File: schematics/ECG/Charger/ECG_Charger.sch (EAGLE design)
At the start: 7 parts, among them IC1 MCP73832_SOT23-5

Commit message: routed charger board
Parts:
- added C2: 4.7uF, rcl:C-USC0805
- added CONN1: M80-4V, harwin:M80-4V
- added CONN2: M80-6V, harwin:M80-6V
- C1: device rcl:C-USC0402 -> rcl:C-USC0805
- R1, R2: device rcl:R-US_R0201 -> rcl:R-US_R0805
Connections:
- removed net VSS: R2.1
- net BATT: now also C2.1, CONN1.3
- net GND: now also C2.2, CONN1.4, R2.1
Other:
- moved on the sheet: C1, FUSE, IC1, LED1, R1, R2, USBCONN

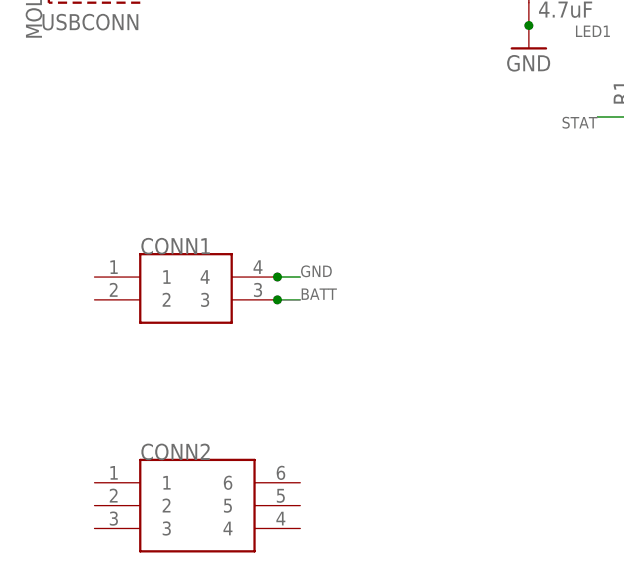
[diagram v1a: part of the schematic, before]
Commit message: switched ECG boards to spring loaded pin headers
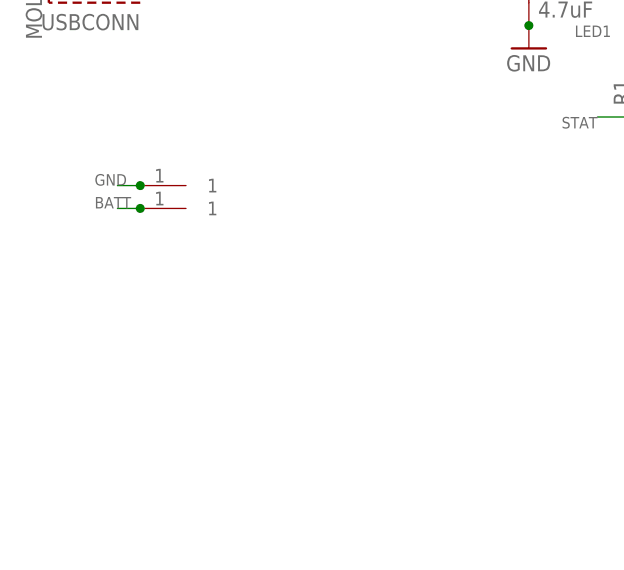
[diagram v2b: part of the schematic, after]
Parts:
- removed CONN1: M80-4V, harwin:M80-4V
- removed CONN2: M80-6V, harwin:M80-6V
- added U$1, U$2: PISTON_RA_TH, pins:PISTON_RA_TH
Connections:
- net BATT: now also U$1.1; no longer CONN1.3
- net GND: now also U$2.1; no longer CONN1.4
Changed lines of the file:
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@@
 <?xml version="1.0" encoding="utf-8"?>
 <!DOCTYPE eagle SYSTEM "eagle.dtd">
-<eagle version="6.4">
+<eagle version="6.5.0">
 <drawing>
 <settings>
@@
 <grid distance="0.1" unitdist="inch" unit="inch" style="lines" multiple="1" display="no" altdistance="0.01" altunitdist="inch" altunit="inch"/>
 <layers>
-<layer number="1" name="Top" color="4" fill="1" visible="yes" active="no"/>
-<layer number="2" name="Route2" color="1" fill="3" visible="yes" active="no"/>
-<layer number="3" name="Route3" color="4" fill="3" visible="yes" active="no"/>
-<layer number="4" name="Route4" color="1" fill="4" visible="yes" active="no"/>
-<layer number="5" name="Route5" color="4" fill="4" visible="yes" active="no"/>
-<layer number="6" name="Route6" color="1" fill="8" visible="yes" active="no"/>
-<layer number="7" name="Route7" color="4" fill="8" visible="yes" active="no"/>
-<layer number="8" name="Route8" color="1" fill="2" visible="yes" active="no"/>
-<layer number="9" name="Route9" color="4" fill="2" visible="yes" active="no"/>
-<layer number="10" name="Route10" color="1" fill="7" visible="yes" active="no"/>
-<layer number="11" name="Route11" color="4" fill="7" visible="yes" active="no"/>
-<layer number="12" name="Route12" color="1" fill="5" visible="yes" active="no"/>
-<layer number="13" name="Route13" color="4" fill="5" visible="yes" active="no"/>
-<layer number="14" name="Route14" color="1" fill="6" visible="yes" active="no"/>
-<layer number="15" name="Route15" color="4" fill="6" visible="yes" active="no"/>
-<layer number="16" name="Bottom" color="1" fill="1" visible="yes" active="no"/>
-<layer number="17" name="Pads" color="2" fill="1" visible="yes" active="no"/>
-<layer number="18" name="Vias" color="2" fill="1" visible="yes" active="no"/>
-<layer number="19" name="Unrouted" color="6" fill="1" visible="yes" active="no"/>
-<layer number="20" name="Dimension" color="15" fill="1" visible="yes" active="no"/>
-<layer number="21" name="tPlace" color="7" fill="1" visible="yes" active="no"/>
-<layer number="22" name="bPlace" color="7" fill="1" visible="yes" active="no"/>
-<layer number="23" name="tOrigins" color="15" fill="1" visible="yes" active="no"/>
-<layer number="24" name="bOrigins" color="15" fill="1" visible="yes" active="no"/>
-<layer number="25" name="tNames" color="7" fill="1" visible="yes" active="no"/>
-<layer number="26" name="bNames" color="7" fill="1" visible="yes" active="no"/>
-<layer number="27" name="tValues" color="7" fill="1" visible="yes" active="no"/>
-<layer number="28" name="bValues" color="7" fill="1" visible="yes" active="no"/>
+<layer number="1" name="Top" color="4" fill="1" visible="no" active="no"/>
+<layer number="2" name="Route2" color="1" fill="3" visible="no" active="no"/>
+<layer number="3" name="Route3" color="4" fill="3" visible="no" active="no"/>
+<layer number="4" name="Route4" color="1" fill="4" visible="no" active="no"/>
+<layer number="5" name="Route5" color="4" fill="4" visible="no" active="no"/>
+<layer number="6" name="Route6" color="1" fill="8" visible="no" active="no"/>
+<layer number="7" name="Route7" color="4" fill="8" visible="no" active="no"/>
+<layer number="8" name="Route8" color="1" fill="2" visible="no" active="no"/>
+<layer number="9" name="Route9" color="4" fill="2" visible="no" active="no"/>
+<layer number="10" name="Route10" color="1" fill="7" visible="no" active="no"/>
+<layer number="11" name="Route11" color="4" fill="7" visible="no" active="no"/>
+<layer number="12" name="Route12" color="1" fill="5" visible="no" active="no"/>
+<layer number="13" name="Route13" color="4" fill="5" visible="no" active="no"/>
+<layer number="14" name="Route14" color="1" fill="6" visible="no" active="no"/>
+<layer number="15" name="Route15" color="4" fill="6" visible="no" active="no"/>
+<layer number="16" name="Bottom" color="1" fill="1" visible="no" active="no"/>
+<layer number="17" name="Pads" color="2" fill="1" visible="no" active="no"/>
+<layer number="18" name="Vias" color="2" fill="1" visible="no" active="no"/>
+<layer number="19" name="Unrouted" color="6" fill="1" visible="no" active="no"/>
+<layer number="20" name="Dimension" color="15" fill="1" visible="no" active="no"/>
+<layer number="21" name="tPlace" color="7" fill="1" visible="no" active="no"/>
+<layer number="22" name="bPlace" color="7" fill="1" visible="no" active="no"/>
+<layer number="23" name="tOrigins" color="15" fill="1" visible="no" active="no"/>
+<layer number="24" name="bOrigins" color="15" fill="1" visible="no" active="no"/>
+<layer number="25" name="tNames" color="7" fill="1" visible="no" active="no"/>
+<layer number="26" name="bNames" color="7" fill="1" visible="no" active="no"/>
+<layer number="27" name="tValues" color="7" fill="1" visible="no" active="no"/>
+<layer number="28" name="bValues" color="7" fill="1" visible="no" active="no"/>
 <layer number="29" name="tStop" color="7" fill="3" visible="no" active="no"/>
 <layer number="30" name="bStop" color="7" fill="6" visible="no" active="no"/>
@@
 <layer number="35" name="tGlue" color="7" fill="4" visible="no" active="no"/>
 <layer number="36" name="bGlue" color="7" fill="5" visible="no" active="no"/>
-<layer number="37" name="tTest" color="7" fill="1" visible="yes" active="no"/>
-<layer number="38" name="bTest" color="7" fill="1" visible="yes" active="no"/>
+<layer number="37" name="tTest" color="7" fill="1" visible="no" active="no"/>
+<layer number="38" name="bTest" color="7" fill="1" visible="no" active="no"/>
 <layer number="39" name="tKeepout" color="4" fill="11" visible="no" active="no"/>
 <layer number="40" name="bKeepout" color="1" fill="11" visible="no" active="no"/>
@@
 <layer number="44" name="Drills" color="7" fill="1" visible="no" active="no"/>
 <layer number="45" name="Holes" color="7" fill="1" visible="no" active="no"/>
-<layer number="46" name="Milling" color="3" fill="1" visible="yes" active="no"/>
-<layer number="47" name="Measures" color="7" fill="1" visible="yes" active="no"/>
-<layer number="48" name="Document" color="7" fill="1" visible="yes" active="no"/>
-<layer number="49" name="Reference" color="7" fill="1" visible="yes" active="no"/>
-<layer number="50" name="dxf" color="7" fill="1" visible="yes" active="no"/>
-<layer number="51" name="tDocu" color="7" fill="1" visible="yes" active="no"/>
-<layer number="52" name="bDocu" color="7" fill="1" visible="yes" active="no"/>
-<layer number="53" name="tGND_GNDA" color="7" fill="9" visible="yes" active="no"/>
-<layer number="54" name="bGND_GNDA" color="1" fill="9" visible="yes" active="no"/>
-<layer number="56" name="wert" color="7" fill="1" visible="yes" active="no"/>
+<layer number="46" name="Milling" color="3" fill="1" visible="no" active="no"/>
+<layer number="47" name="Measures" color="7" fill="1" visible="no" active="no"/>
+<layer number="48" name="Document" color="7" fill="1" visible="no" active="no"/>
+<layer number="49" name="Reference" color="7" fill="1" visible="no" active="no"/>
+<layer number="50" name="dxf" color="7" fill="1" visible="no" active="no"/>
+<layer number="51" name="tDocu" color="7" fill="1" visible="no" active="no"/>
+<layer number="52" name="bDocu" color="7" fill="1" visible="no" active="no"/>
+<layer number="53" name="tGND_GNDA" color="7" fill="9" visible="no" active="no"/>
+<layer number="54" name="bGND_GNDA" color="1" fill="9" visible="no" active="no"/>
+<layer number="56" name="wert" color="7" fill="1" visible="no" active="no"/>
 <layer number="91" name="Nets" color="2" fill="1" visible="yes" active="yes"/>
 <layer number="92" name="Busses" color="1" fill="1" visible="yes" active="yes"/>
@@
 <part name="C2" library="rcl" deviceset="C-US" device="C0805" value="4.7uF"/>
 <part name="GND1" library="supply1" deviceset="GND" device=""/>
-<part name="CONN2" library="harwin" deviceset="M80-6" device="V"/>
-<part name="CONN1" library="harwin" deviceset="M80-4" device="V"/>
 <part name="GND3" library="supply1" deviceset="GND" device=""/>
+<part name="U$1" library="pins" deviceset="PISTON_RA_TH" device=""/>
+<part name="U$2" library="pins" deviceset="PISTON_RA_TH" device=""/>
 </parts>
 <sheets>
@@
 <instance part="C2" gate="G$1" x="198.12" y="121.92"/>
 <instance part="GND1" gate="1" x="198.12" y="114.3"/>
-<instance part="CONN2" gate="CONN" x="88.9" y="63.5"/>
-<instance part="CONN1" gate="CONN" x="88.9" y="86.36"/>
 <instance part="GND3" gate="1" x="147.32" y="106.68"/>
+<instance part="U$1" gate="PIN" x="88.9" y="96.52"/>
+<instance part="U$2" gate="PIN" x="88.9" y="99.06"/>
 </instances>
 <busses>
@@
 </segment>
 <segment>
-<pinref part="CONN1" gate="CONN" pin="4"/>
-<wire x1="99.06" y1="88.9" x2="101.6" y2="88.9" width="0.1524" layer="91"/>
-<label x="101.6" y="88.9" size="1.27" layer="95"/>
-<junction x="99.06" y="88.9"/>
-</segment>
-<segment>
 <pinref part="R2" gate="G$1" pin="1"/>
 <pinref part="GND3" gate="1" pin="GND"/>
 <junction x="147.32" y="109.22"/>
+</segment>
+<segment>
+<pinref part="U$2" gate="PIN" pin="1"/>
+<wire x1="83.82" y1="99.06" x2="81.28" y2="99.06" width="0.1524" layer="91"/>
+<junction x="83.82" y="99.06"/>
+<label x="78.74" y="99.06" size="1.27" layer="95"/>
 </segment>
 </net>
@@
 </segment>
 <segment>
-<pinref part="CONN1" gate="CONN" pin="3"/>
-<wire x1="99.06" y1="86.36" x2="101.6" y2="86.36" width="0.1524" layer="91"/>
-<junction x="99.06" y="86.36"/>
-<label x="101.6" y="86.36" size="1.27" layer="95"/>
-</segment>
-</net>
+<pinref part="U$1" gate="PIN" pin="1"/>
+<wire x1="83.82" y1="96.52" x2="81.28" y2="96.52" width="0.1524" layer="91"/>
+<junction x="83.82" y="96.52"/>
+<label x="78.74" y="96.52" size="1.27" layer="95"/>
+</segment>
+</net>

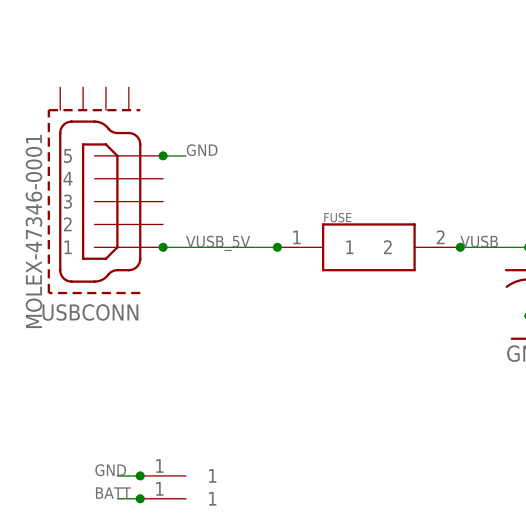
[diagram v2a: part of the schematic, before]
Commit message: changed micro USB port
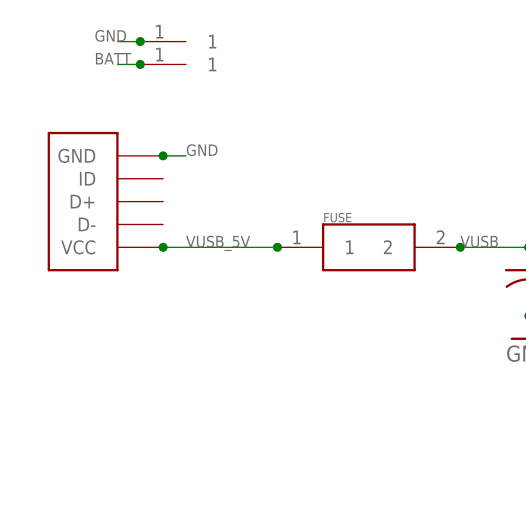
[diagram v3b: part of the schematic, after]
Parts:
- removed USBCONN: MOLEX-47346-0001, usb_con-update:MOLEX-47346-0001
- added J1: USB_MICROC, KomodoOpenLab:USB_MICROC
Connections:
- net GND: now also J1.GND; no longer USBCONN.5
- net VUSB_5V: now also J1.VCC; no longer USBCONN.1
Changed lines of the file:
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@@
 <part name="LED1" library="LITEON" deviceset="LED_SMT_0805" device=""/>
 <part name="R1" library="rcl" deviceset="R-US_" device="R0805" value="470"/>
-<part name="USBCONN" library="usb_con-update" deviceset="MOLEX-47346-0001" device=""/>
 <part name="FUSE" library="bourns-fuse" deviceset="FUSE-MF_SERIES" device=""/>
 <part name="C2" library="rcl" deviceset="C-US" device="C0805" value="4.7uF"/>
@@
 <part name="U$1" library="pins" deviceset="PISTON_RA_TH" device=""/>
 <part name="U$2" library="pins" deviceset="PISTON_RA_TH" device=""/>
+<part name="J1" library="KomodoOpenLab" deviceset="USB_MICROC" device=""/>
 </parts>
 <sheets>
@@
 <instance part="LED1" gate="LED" x="139.7" y="121.92" rot="MR0"/>
 <instance part="R1" gate="G$1" x="139.7" y="111.76" rot="R90"/>
-<instance part="USBCONN" gate="G$1" x="81.28" y="129.54" rot="R180"/>
 <instance part="FUSE" gate="FUSE" x="109.22" y="124.46"/>
 <instance part="C2" gate="G$1" x="198.12" y="121.92"/>
 <instance part="GND1" gate="1" x="198.12" y="114.3"/>
 <instance part="GND3" gate="1" x="147.32" y="106.68"/>
-<instance part="U$1" gate="PIN" x="88.9" y="96.52"/>
-<instance part="U$2" gate="PIN" x="88.9" y="99.06"/>
+<instance part="U$1" gate="PIN" x="88.9" y="144.78"/>
+<instance part="U$2" gate="PIN" x="88.9" y="147.32"/>
+<instance part="J1" gate="G$1" x="81.28" y="134.62" rot="R180"/>
 </instances>
 <busses>
@@
 <segment>
 <wire x1="86.36" y1="134.62" x2="88.9" y2="134.62" width="0.1524" layer="91"/>
+<label x="88.9" y="134.62" size="1.27" layer="95"/>
+<pinref part="J1" gate="G$1" pin="GND"/>
 <junction x="86.36" y="134.62"/>
-<pinref part="USBCONN" gate="G$1" pin="5"/>
-<label x="88.9" y="134.62" size="1.27" layer="95"/>
 </segment>
 <segment>
@@
 <segment>
 <pinref part="U$2" gate="PIN" pin="1"/>
-<wire x1="83.82" y1="99.06" x2="81.28" y2="99.06" width="0.1524" layer="91"/>
-<junction x="83.82" y="99.06"/>
-<label x="78.74" y="99.06" size="1.27" layer="95"/>
+<wire x1="83.82" y1="147.32" x2="81.28" y2="147.32" width="0.1524" layer="91"/>
+<junction x="83.82" y="147.32"/>
+<label x="78.74" y="147.32" size="1.27" layer="95"/>
 </segment>
 </net>
@@
 <segment>
 <wire x1="99.06" y1="124.46" x2="86.36" y2="124.46" width="0.1524" layer="91"/>
-<junction x="86.36" y="124.46"/>
 <junction x="99.06" y="124.46"/>
 <label x="88.9" y="124.46" size="1.27" layer="95"/>
-<pinref part="USBCONN" gate="G$1" pin="1"/>
 <pinref part="FUSE" gate="FUSE" pin="1"/>
+<pinref part="J1" gate="G$1" pin="VCC"/>
+<junction x="86.36" y="124.46"/>
 </segment>
 </net>
@@
 <segment>
 <pinref part="U$1" gate="PIN" pin="1"/>
-<wire x1="83.82" y1="96.52" x2="81.28" y2="96.52" width="0.1524" layer="91"/>
-<junction x="83.82" y="96.52"/>
-<label x="78.74" y="96.52" size="1.27" layer="95"/>
+<wire x1="83.82" y1="144.78" x2="81.28" y2="144.78" width="0.1524" layer="91"/>
+<junction x="83.82" y="144.78"/>
+<label x="78.74" y="144.78" size="1.27" layer="95"/>
 </segment>
 </net>

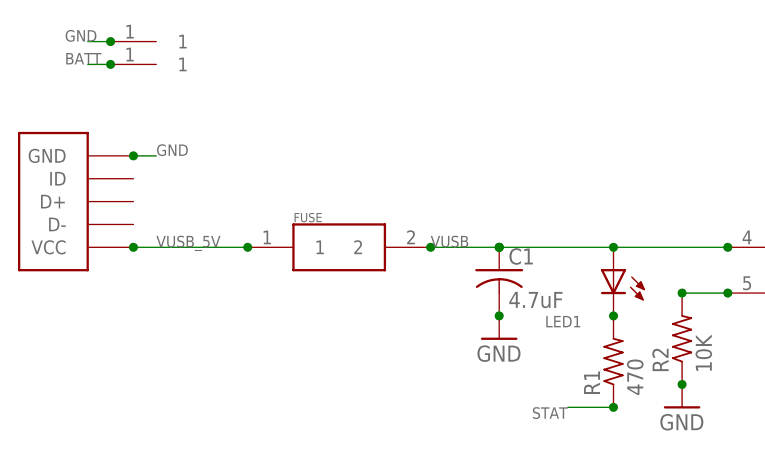
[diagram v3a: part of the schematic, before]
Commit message: shrunk caps and resistors to 0402 package sizes. Added 124k resistor on ID pin of USB
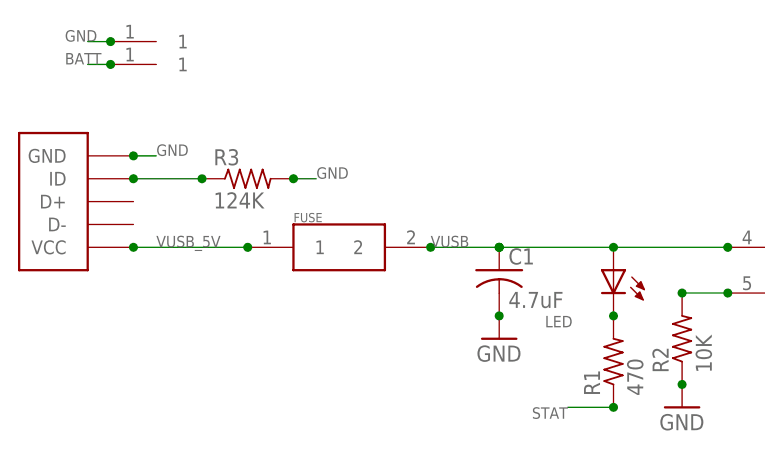
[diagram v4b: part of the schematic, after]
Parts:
- added R3: 124K, rcl:R-US_R0402
- C1, C2: device rcl:C-USC0805 -> rcl:C-USC0402
- R1, R2: device rcl:R-US_R0805 -> rcl:R-US_R0402
- renumbered LED1 to LED
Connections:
- new net N$1: J1.ID, R3.1
- net GND: now also R3.2
